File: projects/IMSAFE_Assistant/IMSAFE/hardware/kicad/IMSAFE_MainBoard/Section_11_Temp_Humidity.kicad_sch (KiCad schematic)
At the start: 0 parts

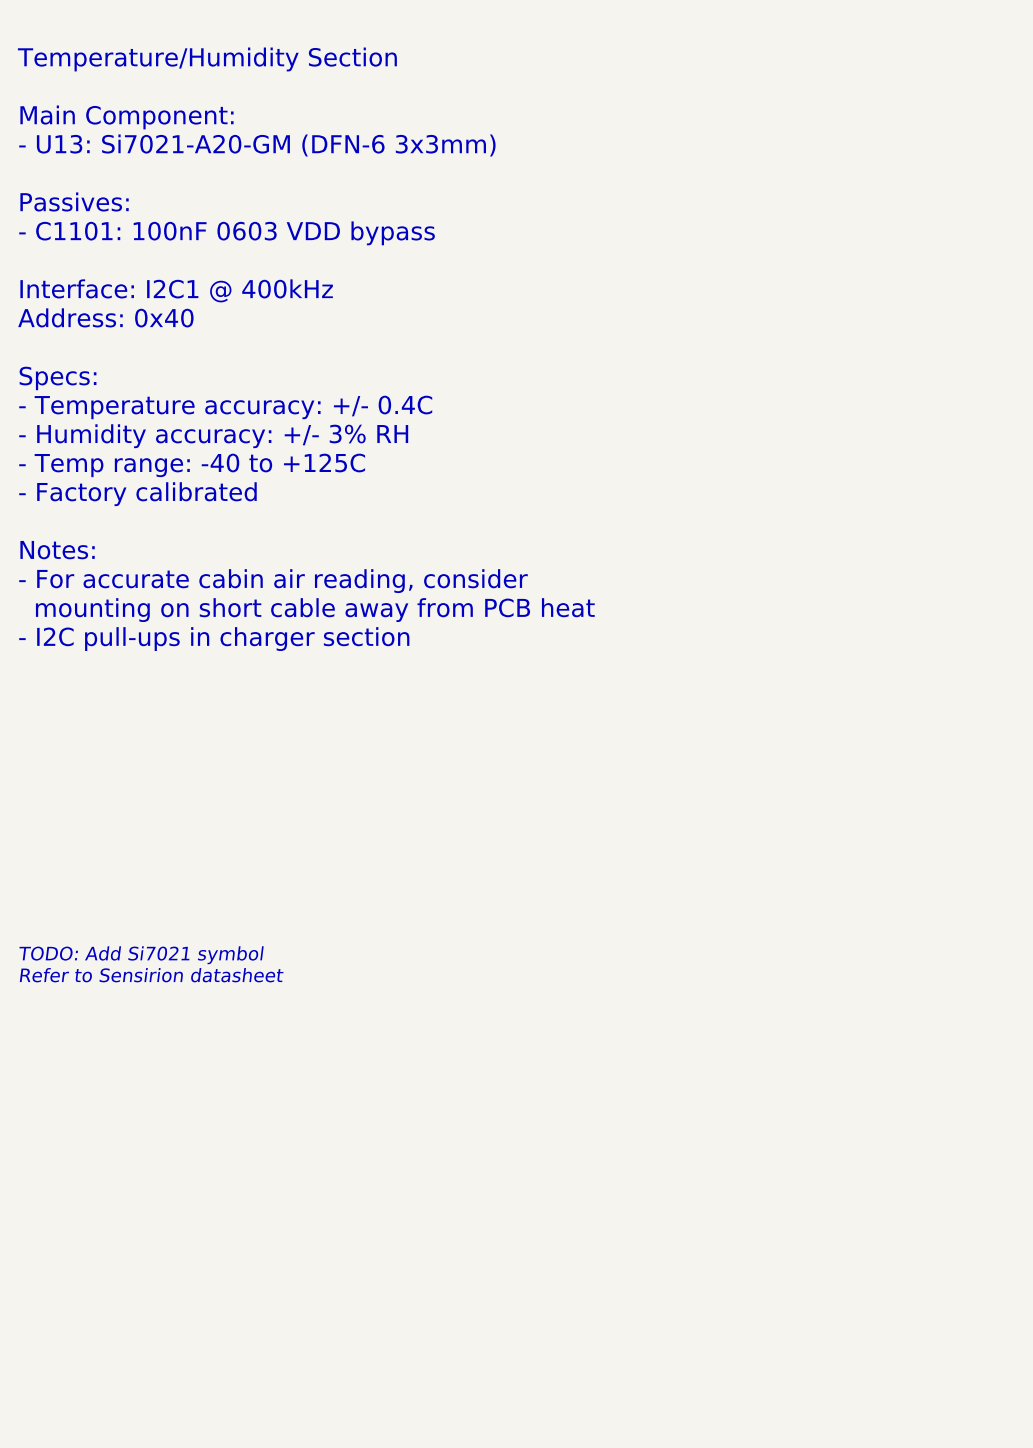
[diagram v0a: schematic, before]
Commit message: Add sensor and interface schematic implementations
- Section 01: MCU Core additional connections
- Section 04: BMS refinements
- Section 07: Barometric sensor (BMP390)
- Section 08: IMU (ICM-42688-P) full implementation
- Section 09: Magnetometer (MMC5983MA) full implementation
- Section 10: Gas sensor (MICS-4514) with heater control
- Section 11: Temp/Humidity (Si7021-A20) implementation
- Section 14: I/O Expander updates
- Section 16: Rotary encoder connections
- Section 19: Audio buzzer (MLT-8530) with MOSFET driver

Co-Authored-By: Claude Opus 4.5 <noreply@anthropic.com>
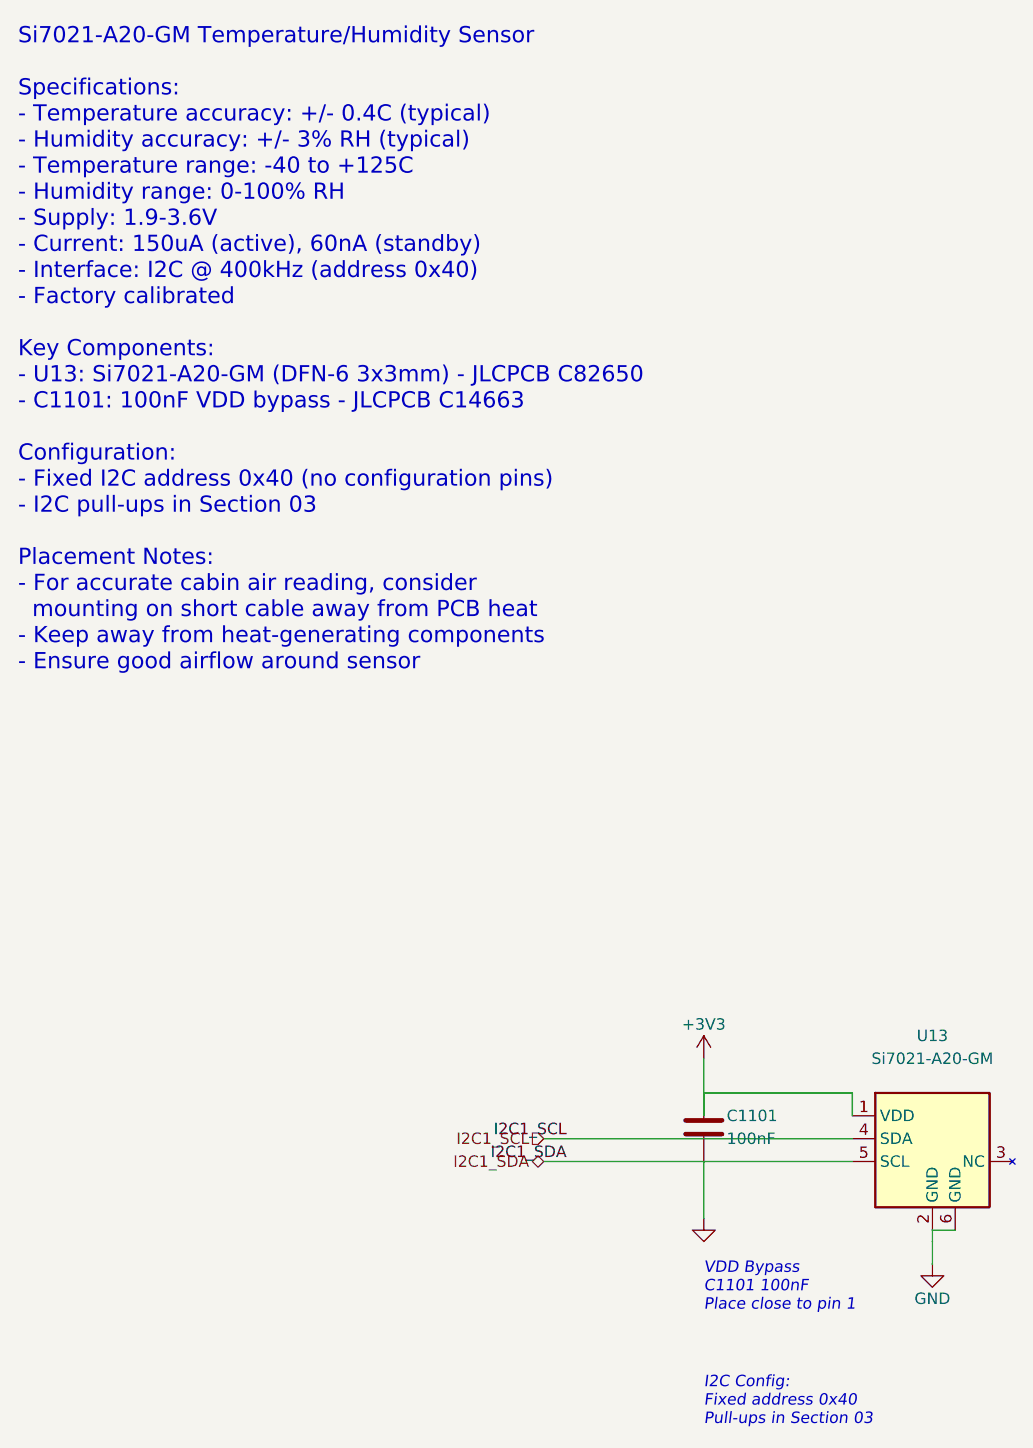
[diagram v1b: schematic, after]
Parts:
- added C1101: 100nF, Capacitor_SMD:C_0603_1608Metric, symbol Device:C
- added U13: Si7021-A20-GM, Package_DFN_QFN:DFN-6-1EP_3x3mm_P1mm_EP1.5x2.4mm, symbol Sensor:Si7021-A20
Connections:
- new net +3V3: C1101.1, U13.1 (VDD)
- new net GND: C1101.2, U13.2 (GND), U13.6 (GND)
- new net I2C1_SCL: U13.4 (SDA)
- new net I2C1_SDA: U13.5 (SCL)
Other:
- note added: "I2C Config: Fixed address 0x40 Pull-ups in Section 03"
- note added: "Si7021-A20-GM Temperature/Humidity Sensor Specifications: - Temperature accuracy: +/- 0.4C (typical) - Humidity accuracy: +/- 3% RH (typical) - Temperature range: -40 to +125C - Humidity range: 0-100% RH - Supply: 1.9-3.6V - Current: 150uA (active), 60nA (standby) - Interface: I2C @ 400kHz (address 0x40) - Factory calibrated Key Components: - U13: Si7021-A20-GM (DFN-6 3x3mm) - JLCPCB C82650 - C11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"
- note added: "VDD Bypass C1101 100nF Place close to pin 1"
- note removed: "TODO: Add Si7021 symbol Refer to Sensirion datasheet"
- note removed: "Temperature/Humidity Section Main Component: - U13: Si7021-A20-GM (DFN-6 3x3mm) Passives: - C1101: 100nF 0603 VDD bypass Interface: I2C1 @ 400kHz Address: 0x40 Specs: - Temperature accuracy: +/- 0.4C - Humidity accuracy: +/- 3% RH - Temp range: -40 to +125C - Factory calibrated Notes: - For accurate cabin air reading, consider mounting on short cable away from PCB heat - I2C pull-ups in charger s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"
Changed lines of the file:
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@@
 	(title_block
 		(title "Section 11: Temperature & Humidity")
-		(date "2026-01-28")
-		(rev "0.1")
+		(date "2026-01-29")
+		(rev "1.0")
 		(company "IMSAFE Project")
-		(comment 1 "Si7021 Temp/Humidity Sensor")
-		(comment 2 "I2C address 0x40")
+		(comment 1 "Si7021-A20-GM Temperature/Humidity Sensor")
+		(comment 2 "I2C address 0x40 (fixed)")
 	)
-	(text "Temperature/Humidity Section\n\nMain Component:\n- U13: Si7021-A20-GM (DFN-6 3x3mm)\n\nPassives:\n- C1101: 100nF 0603 VDD bypass\n\nInterface: I2C1 @ 400kHz\nAddress: 0x40\n\nSpecs:\n- Temperature accuracy: +/- 0.4C\n- Humidity accuracy: +/- 3% RH\n- Temp range: -40 to +125C\n- Factory calibrated\n\nNotes:\n- For accurate cabin air reading, consider\n  mounting on short cable away from PCB heat\n- I2C pull-ups in charger section"
+	(text "Si7021-A20-GM Temperature/Humidity Sensor\n\nSpecifications:\n- Temperature accuracy: +/- 0.4C (typical)\n- Humidity accuracy: +/- 3% RH (typical)\n- Temperature range: -40 to +125C\n- Humidity range: 0-100% RH\n- Supply: 1.9-3.6V\n- Current: 150uA (active), 60nA (standby)\n- Interface: I2C @ 400kHz (address 0x40)\n- Factory calibrated\n\nKey Components:\n- U13: Si7021-A20-GM (DFN-6 3x3mm) - JLCPCB C82650\n- C1101: 100nF VDD bypass - JLCPCB C14663\n\nConfiguration:\n- Fixed I2C address 0x40 (no configuration pins)\n- I2C pull-ups in Section 03\n\nPlacement Notes:\n- For accurate cabin air reading, consider\n  mounting on short cable away from PCB heat\n- Keep away from heat-generating components\n- Ensure good airflow around sensor"
 		(exclude_from_sim no)
 		(at 25.4 25.4 0)
-		(effects
-			(font
-				(size 2 2)
-			)
-			(justify left)
-		)
+		(effects (font (size 1.8 1.8)) (justify left))
 		(uuid "sec11-text-001")
 	)
-	(text "TODO: Add Si7021 symbol\nRefer to Sensirion datasheet"
+	(symbol (lib_id "Sensor:Si7021-A20") (at 127 114.3 0) (unit 1)
+		(exclude_from_sim no) (in_bom yes) (on_board yes) (dnp no)
+		(uuid "u13-si7021-uuid")
+		(property "Reference" "U13" (at 127 101.6 0) (effects (font (size 1.27 1.27))))
+		(property "Value" "Si7021-A20-GM" (at 127 104.14 0) (effects (font (size 1.27 1.27))))
+		(property "Footprint" "Package_DFN_QFN:DFN-6-1EP_3x3mm_P1mm_EP1.5x2.4mm" (at 127 127 0) (effects (font (size 1.27 1.27)) hide))
+		(property "Datasheet" "https://www.silabs.com/documents/public/data-sheets/Si7021-A20.pdf" (at 127 114.3 0) (effects (font (size 1.27 1.27)) hide))
+		(property "JLCPCB" "C82650" (at 127 114.3 0) (effects (font (size 1.27 1.27)) hide))
+		(pin "1" (uuid "u13-vdd")) (pin "2" (uuid "u13-gnd1")) (pin "3" (uuid "u13-nc"))
+		(pin "4" (uuid "u13-sda")) (pin "5" (uuid "u13-scl")) (pin "6" (uuid "u13-gnd2"))
+		(instances (project "IMSAFE_MainBoard" (path "/sec11-0001-0002-0003-000000000001" (reference "U13") (unit 1))))
+	)
+	(symbol (lib_id "Device:C") (at 101.6 111.76 0) (unit 1)
+		(exclude_from_sim no) (in_bom yes) (on_board yes) (dnp no)
+		(uuid "c1101-uuid")
+		(property "Reference" "C1101" (at 104.14 110.49 0) (effects (font (size 1.27 1.27)) (justify left)))
+		(property "Value" "100nF" (at 104.14 113.03 0) (effects (font (size 1.27 1.27)) (justify left)))
+		(property "Footprint" "Capacitor_SMD:C_0603_1608Metric" (at 102.5652 115.57 0) (effects (font (size 1.27 1.27)) hide))
+		(property "Datasheet" "~" (at 101.6 111.76 0) (effects (font (size 1.27 1.27)) hide))
+		(property "JLCPCB" "C14663" (at 101.6 111.76 0) (effects (font (size 1.27 1.27)) hide))
+		(pin "1" (uuid "c1101-p1")) (pin "2" (uuid "c1101-p2"))
+		(instances (project "IMSAFE_MainBoard" (path "/sec11-0001-0002-0003-000000000001" (reference "C1101") (unit 1))))
+	)
+	(symbol (lib_id "power:+3V3") (at 101.6 104.14 0) (unit 1)
+		(exclude_from_sim no) (in_bom yes) (on_board yes) (dnp no)
+		(uuid "pwr-3v3-vdd")
+		(property "Reference" "#PWR1101" (at 101.6 107.95 0) (effects (font (size 1.27 1.27)) hide))
+		(property "Value" "+3V3" (at 101.6 100.33 0) (effects (font (size 1.27 1.27))))
+		(property "Footprint" "" (at 101.6 104.14 0) (effects (font (size 1.27 1.27)) hide))
+		(property "Datasheet" "" (at 101.6 104.14 0) (effects (font (size 1.27 1.27)) hide))
+		(pin "1" (uuid "pwr-3v3-vdd-p1"))
+		(instances (project "IMSAFE_MainBoard" (path "/sec11-0001-0002-0003-000000000001" (reference "#PWR1101") (unit 1))))
+	)
+	(symbol (lib_id "power:GND") (at 127 127 0) (unit 1)
+		(exclude_from_sim no) (in_bom yes) (on_board yes) (dnp no)
+		(uuid "pwr-gnd-u13")
+		(property "Reference" "#PWR1102" (at 127 133.35 0) (effects (font (size 1.27 1.27)) hide))
+		(property "Value" "GND" (at 127 130.81 0) (effects (font (size 1.27 1.27))))
+		(property "Footprint" "" (at 127 127 0) (effects (font (size 1.27 1.27)) hide))
+		(property "Datasheet" "" (at 127 127 0) (effects (font (size 1.27 1.27)) hide))
+		(pin "1" (uuid "pwr-gnd-u13-p1"))
+		(instances (project "IMSAFE_MainBoard" (path "/sec11-0001-0002-0003-000000000001" (reference "#PWR1102") (unit 1))))
+	)
+	(symbol (lib_id "power:GND") (at 101.6 121.92 0) (unit 1)
+		(exclude_from_sim no) (in_bom yes) (on_board yes) (dnp no)
+		(uuid "pwr-gnd-c1101")
+		(property "Reference" "#PWR1103" (at 101.6 128.27 0) (effects (font (size 1.27 1.27)) hide))
+		(property "Value" "GND" (at 101.6 125.73 0) (effects (font (size 1.27 1.27)) hide))
+		(property "Footprint" "" (at 101.6 121.92 0) (effects (font (size 1.27 1.27)) hide))
+		(property "Datasheet" "" (at 101.6 121.92 0) (effects (font (size 1.27 1.27)) hide))
+		(pin "1" (uuid "pwr-gnd-c1101-p1"))
+		(instances (project "IMSAFE_MainBoard" (path "/sec11-0001-0002-0003-000000000001" (reference "#PWR1103") (unit 1))))
+	)
+	(wire (pts (xy 101.6 104.14) (xy 101.6 107.95)) (stroke (width 0) (type default)) (uuid "w-3v3-c1101-top"))
+	(wire (pts (xy 101.6 107.95) (xy 101.6 110.49)) (stroke (width 0) (type default)) (uuid "w-vdd-c1101"))
+	(wire (pts (xy 101.6 107.95) (xy 118.11 107.95)) (stroke (width 0) (type default)) (uuid "w-vdd-conn"))
+	(wire (pts (xy 118.11 107.95) (xy 118.11 110.49)) (stroke (width 0) (type default)) (uuid "w-vdd-u13"))
+	(wire (pts (xy 101.6 115.57) (xy 101.6 121.92)) (stroke (width 0) (type default)) (uuid "w-c1101-gnd"))
+	(wire (pts (xy 127 123.19) (xy 127 124.46)) (stroke (width 0) (type default)) (uuid "w-u13-gnd-join1"))
+	(wire (pts (xy 129.54 123.19) (xy 127 123.19)) (stroke (width 0) (type default)) (uuid "w-u13-gnd-join2"))
+	(wire (pts (xy 127 124.46) (xy 127 127)) (stroke (width 0) (type default)) (uuid "w-u13-gnd"))
+	(wire (pts (xy 118.11 115.57) (xy 83.82 115.57)) (stroke (width 0) (type default)) (uuid "w-sda-u13"))
+	(wire (pts (xy 118.11 113.03) (xy 83.82 113.03)) (stroke (width 0) (type default)) (uuid "w-scl-u13"))
+	(label "I2C1_SDA" (at 86.36 115.57 180) (fields_autoplaced yes)
+		(effects (font (size 1.27 1.27)) (justify right bottom))
+		(uuid "label-sda")
+	)
+	(label "I2C1_SCL" (at 86.36 113.03 180) (fields_autoplaced yes)
+		(effects (font (size 1.27 1.27)) (justify right bottom))
+		(uuid "label-scl")
+	)
+	(hierarchical_label "I2C1_SDA" (shape bidirectional) (at 83.82 115.57 180) (fields_autoplaced yes)
+		(effects (font (size 1.27 1.27)) (justify right))
+		(uuid "hl-sda")
+	)
+	(hierarchical_label "I2C1_SCL" (shape input) (at 83.82 113.03 180) (fields_autoplaced yes)
+		(effects (font (size 1.27 1.27)) (justify right))
+		(uuid "hl-scl")
+	)
+	(text "VDD Bypass\nC1101 100nF\nPlace close to pin 1"
 		(exclude_from_sim no)
-		(at 25.4 93.98 0)
-		(effects
-			(font
-				(size 1.5 1.5)
-				(italic yes)
-			)
-			(justify left)
-		)
-		(uuid "sec11-todo-001")
+		(at 101.6 129.54 0)
+		(effects (font (size 1.27 1.27) (italic yes)) (justify left))
+		(uuid "text-c1101")
 	)
+	(text "I2C Config:\nFixed address 0x40\nPull-ups in Section 03"
+		(exclude_from_sim no)
+		(at 101.6 142.24 0)
+		(effects (font (size 1.27 1.27) (italic yes)) (justify left))
+		(uuid "text-i2c-config")
+	)
+	(sheet_instances (path "/" (page "1")))
 )

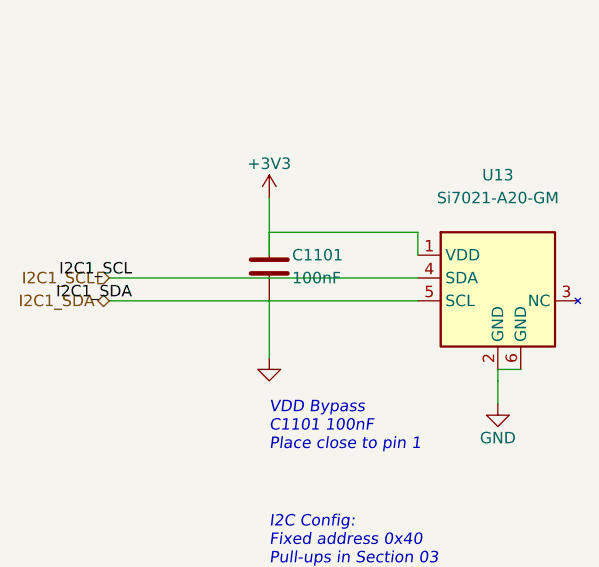
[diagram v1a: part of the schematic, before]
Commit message: Update KiCad schematics and add analysis files
- Update all MainBoard schematic sections with component placement
- Add ERC reports and analysis scripts for schematic validation
- Update Radar Interface and SwitchLED Board projects
- Sync KiCad project files with latest session changes

Co-Authored-By: Claude Opus 4.5 <noreply@anthropic.com>
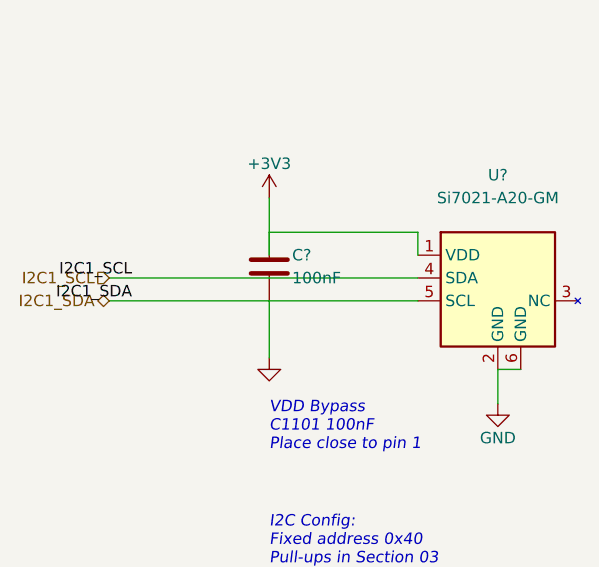
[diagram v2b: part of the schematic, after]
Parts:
- removed C1101: 100nF, Capacitor_SMD:C_0603_1608Metric, symbol Device:C
- removed U13: Si7021-A20-GM, Package_DFN_QFN:DFN-6-1EP_3x3mm_P1mm_EP1.5x2.4mm, symbol Sensor:Si7021-A20
- added C?: 100nF, Capacitor_SMD:C_0603_1608Metric, symbol Device:C
- added U?: Si7021-A20-GM, Package_DFN_QFN:DFN-6-1EP_3x3mm_P1mm_EP1.5x2.4mm, symbol Sensor:Si7021-A20
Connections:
- net +3V3: now also C?.1, U?.1 (VDD)
- net GND: now also C?.2, U?.2 (GND), U?.6 (GND)
- net I2C1_SCL: now also U?.4 (SDA)
- net I2C1_SDA: now also U?.5 (SCL)
